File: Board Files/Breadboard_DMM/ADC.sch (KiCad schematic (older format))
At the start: 22 parts, among them Q201 NTZD3154N, U201 NAU7802, U202 MAX6071x41

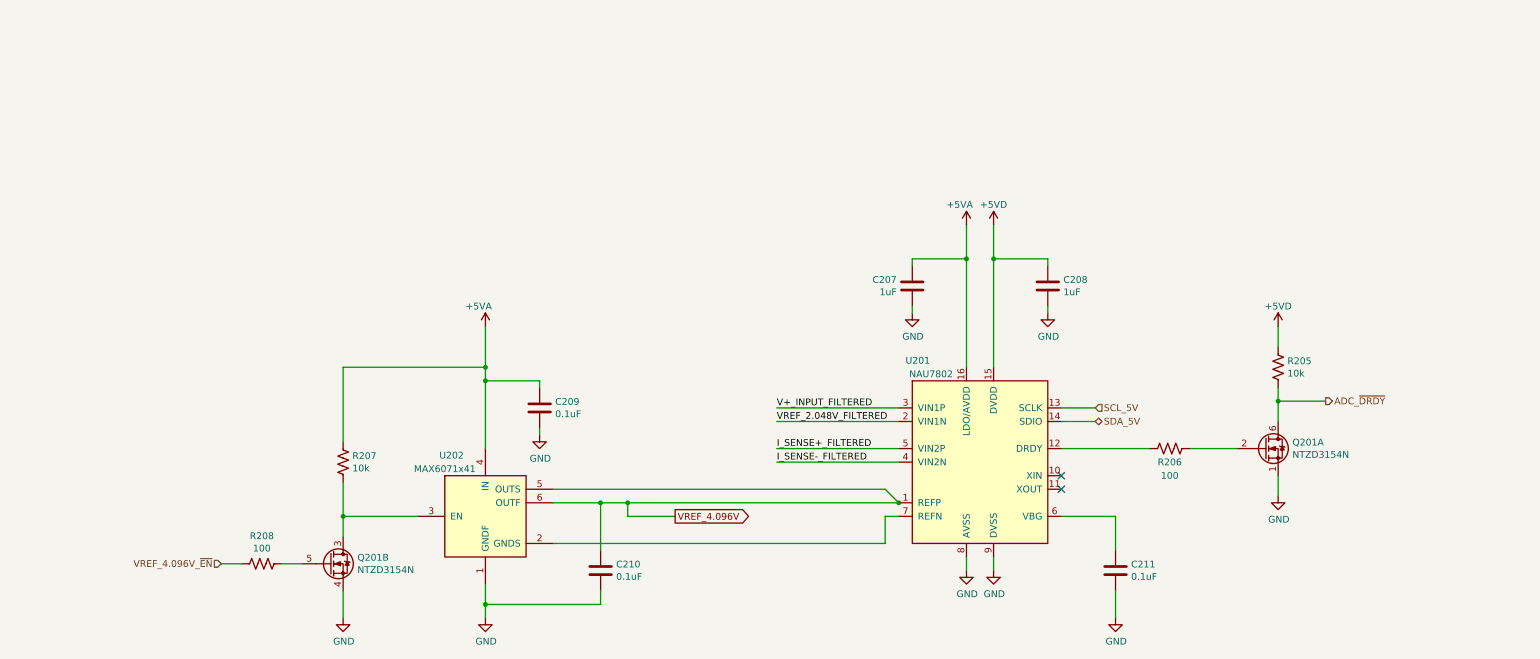
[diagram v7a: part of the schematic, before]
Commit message: Semi-finished component placement
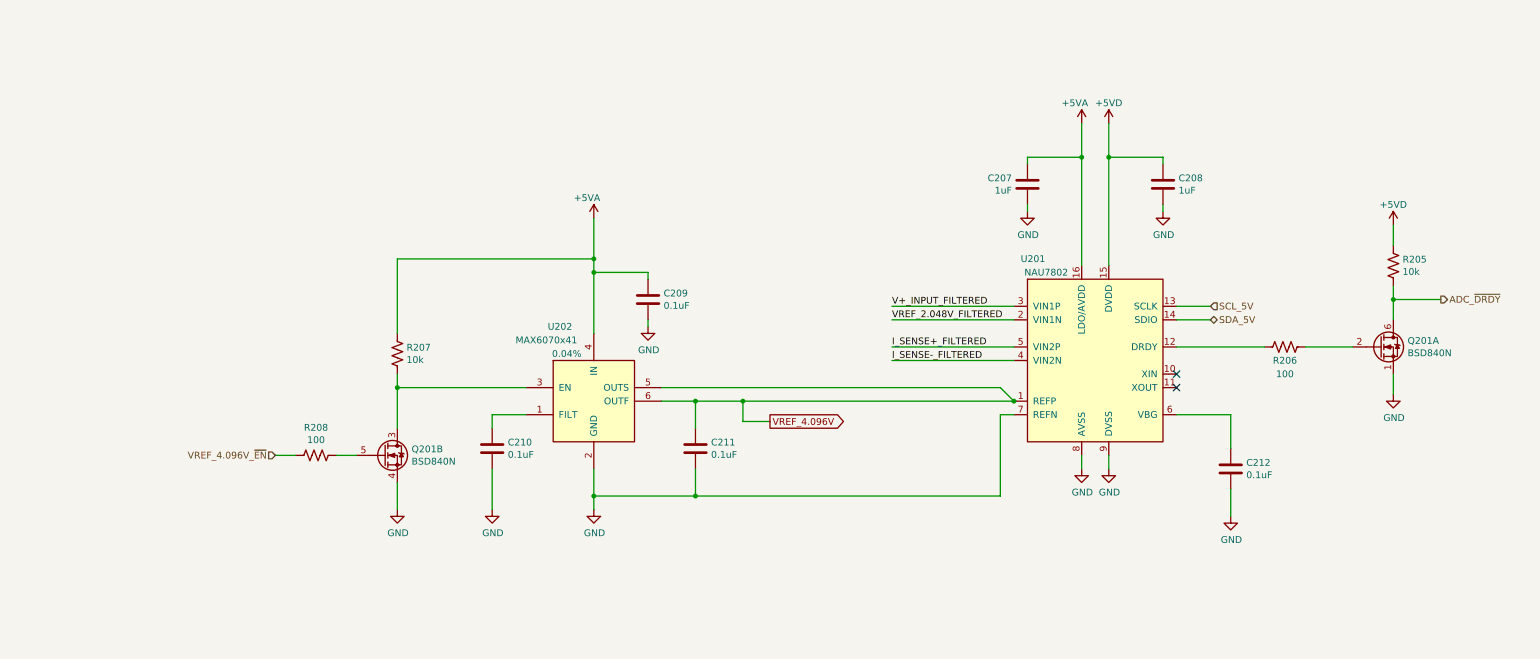
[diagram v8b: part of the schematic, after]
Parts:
- removed U202: MAX6071x41, Package_TO_SOT_SMD:SOT-23-6, symbol irex_Reference_Voltage:MAX6071x41
- added C210: 0.1uF, Capacitor_SMD:C_0603_1608Metric_Pad1.08x0.95mm_HandSolder, symbol Device:C
- added U202: MAX6070x41, Package_TO_SOT_SMD:SOT-23-6, symbol irex_Reference_Voltage:MAX6070x
- C201, C202, C203, C204, C205, C206, C207, C208, C209: footprint Resistor_SMD:R_0603_1608Metric_Pad1.05x0.95mm_HandSolder -> Capacitor_SMD:C_0603_1608Metric_Pad1.08x0.95mm_HandSolder
- C211: renamed from C210; footprint Resistor_SMD:R_0603_1608Metric_Pad1.05x0.95mm_HandSolder -> Capacitor_SMD:C_0603_1608Metric_Pad1.08x0.95mm_HandSolder
- C212: renamed from C211; footprint Resistor_SMD:R_0603_1608Metric_Pad1.05x0.95mm_HandSolder -> Capacitor_SMD:C_0603_1608Metric_Pad1.08x0.95mm_HandSolder
- Q201: value NTZD3154N -> BSD840N; footprint Package_TO_SOT_SMD:SOT-563 -> Package_TO_SOT_SMD:SOT-363_SC-70-6_Handsoldering; Digi-Key Link https://www.digikey.com/en/products/detail/on-semiconductor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 -> https://www.digikey.com/en/products/detail/infineon-technol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; Digi-Key PN NTZD3154NT1GOSCT-ND -> BSD840NH6327XTSA1CT-ND; MPN (none) -> BSD840NH6327XTSA1
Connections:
- net +5VA: now also U202.4 (IN)
- net GND: now also U201.7 (REFN), C210.2, U202.2 (GND)
- net VREF_4.096V: now also U202.5 (OUTS), U202.6 (OUTF)
- net at Q201.3 (D2), R207.1: now also U202.3 (EN)
- new net: C210.1, U202.1 (FILT)
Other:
- moved on the sheet: C207, C208, C209, C211, C212, Q201A, Q201B, R205, R206, R207, R208, U201
